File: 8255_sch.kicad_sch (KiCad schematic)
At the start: 13 parts, among them J1 Conn_01x08_Male, J2 Conn_01x08_Male, J3 Conn_01x08_Male, J4 Conn_01x08_Male, J5 Conn_01x08_Male, J6 Conn_01x08_Male, J7 Conn_01x08_Male, J8 Conn_01x08_Male, J9 Conn_01x08_Male, U2 8255, U5 8255, U6 8255, U7 PAL16L8

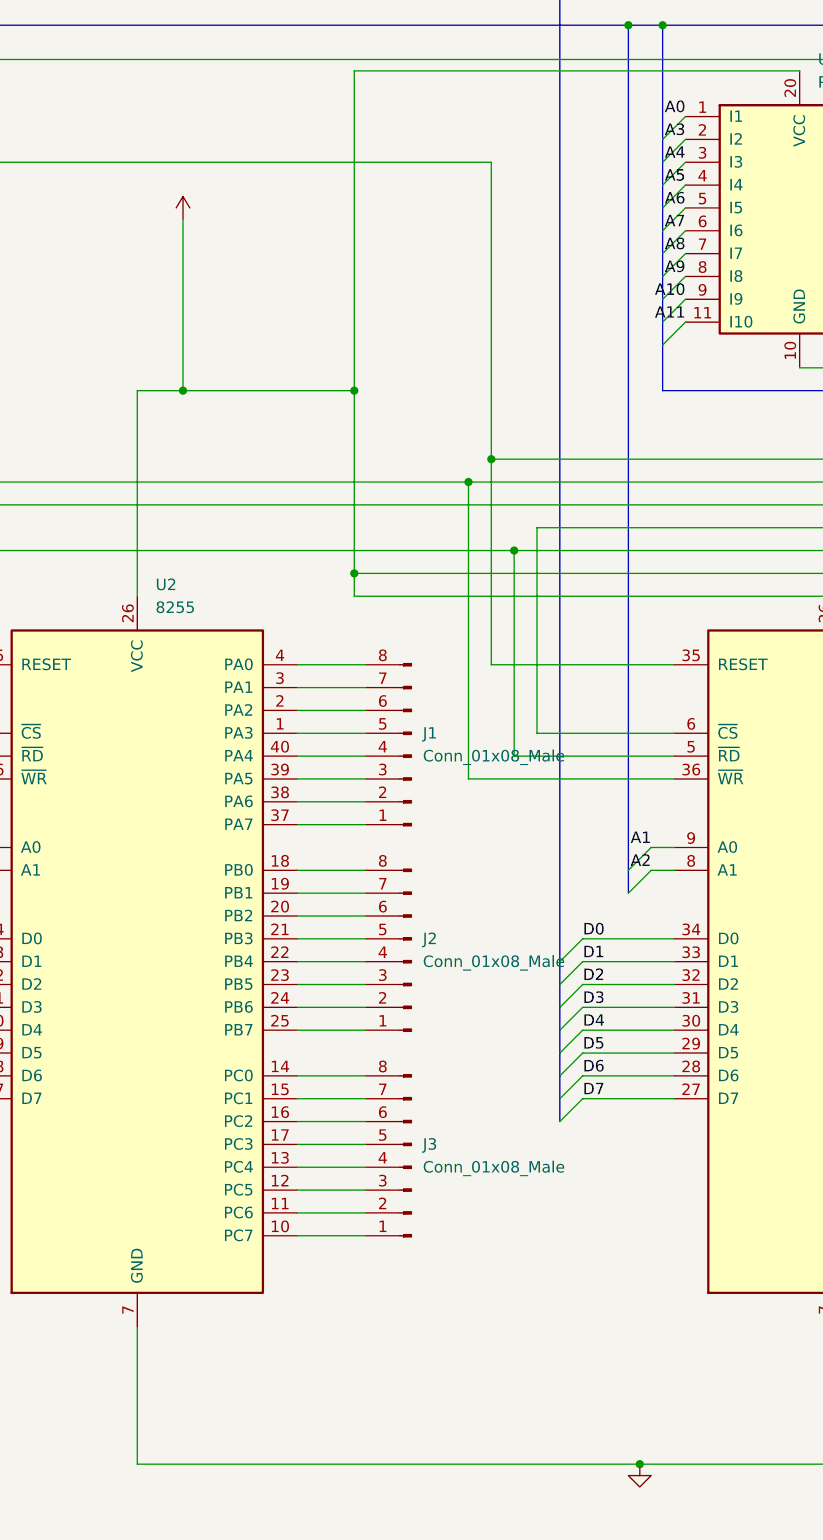
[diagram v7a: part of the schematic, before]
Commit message: Enabled inputs on the max235
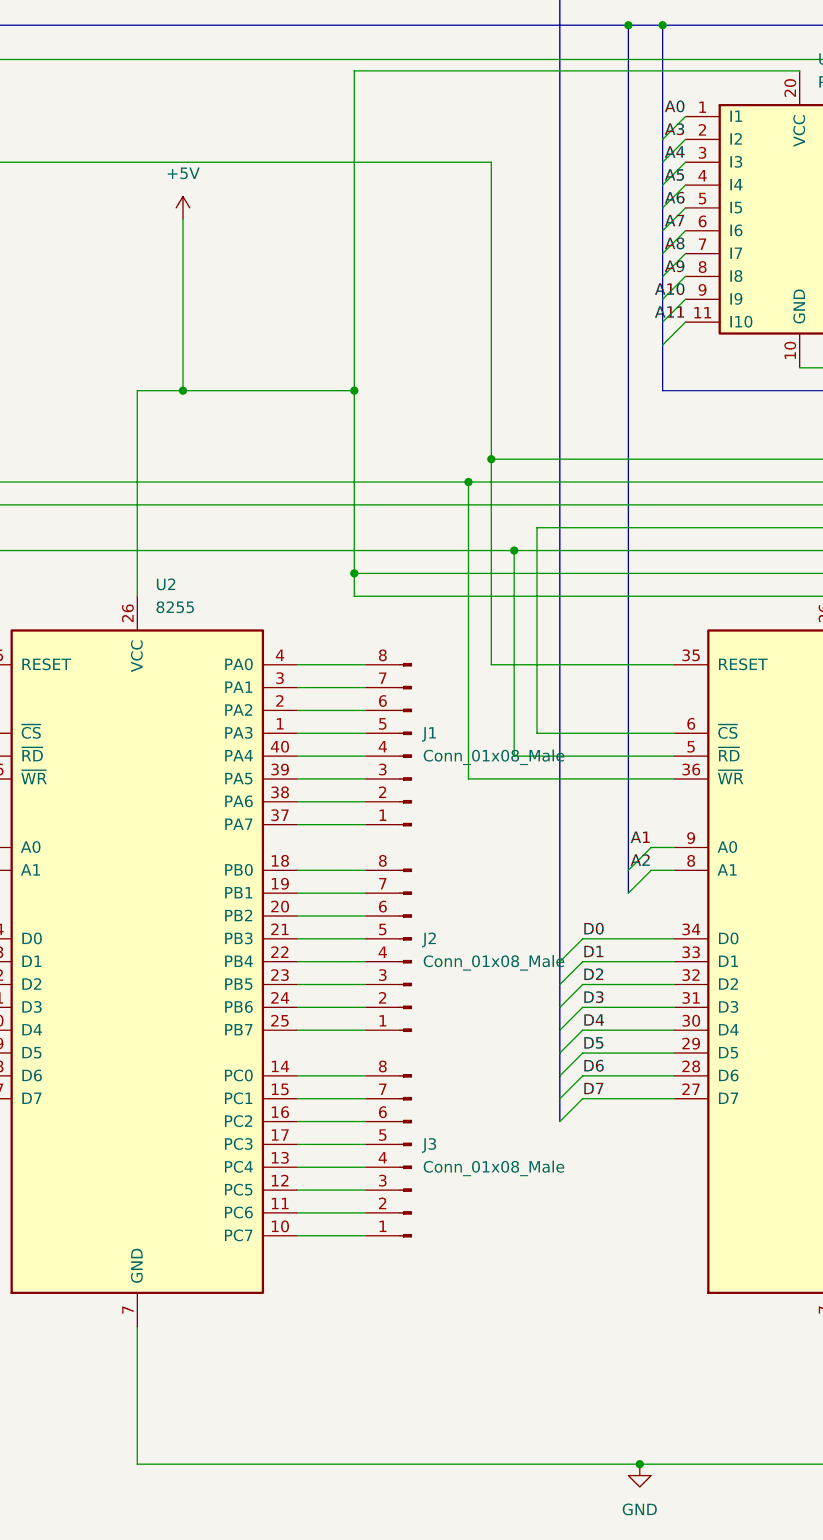
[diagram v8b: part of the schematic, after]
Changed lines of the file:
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@@
       (effects (font (size 1.27 1.27)) hide)
     )
-    (property "Value" "" (id 1) (at 129.54 185.42 0))
+    (property "Value" "GND" (id 1) (at 129.54 185.42 0))
     (property "Footprint" "" (id 2) (at 129.54 180.34 0)
       (effects (font (size 1.27 1.27)) hide)
@@
       (effects (font (size 1.27 1.27)) hide)
     )
-    (property "Value" "" (id 1) (at 78.74 36.83 0))
+    (property "Value" "+5V" (id 1) (at 78.74 36.83 0))
     (property "Footprint" "" (id 2) (at 78.74 41.91 0)
       (effects (font (size 1.27 1.27)) hide)
